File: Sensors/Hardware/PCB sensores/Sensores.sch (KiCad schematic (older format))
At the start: 49 parts, among them J1 Conn_01x02_Female, J2 Conn_01x03, J3 Conn_02x04_Top_Bottom, J4 Conn_01x02_Female, Q1 2N3904, U1 LM324, U2 LM324, U3 ADP1101, U4 MPX10DP, U5 LM358

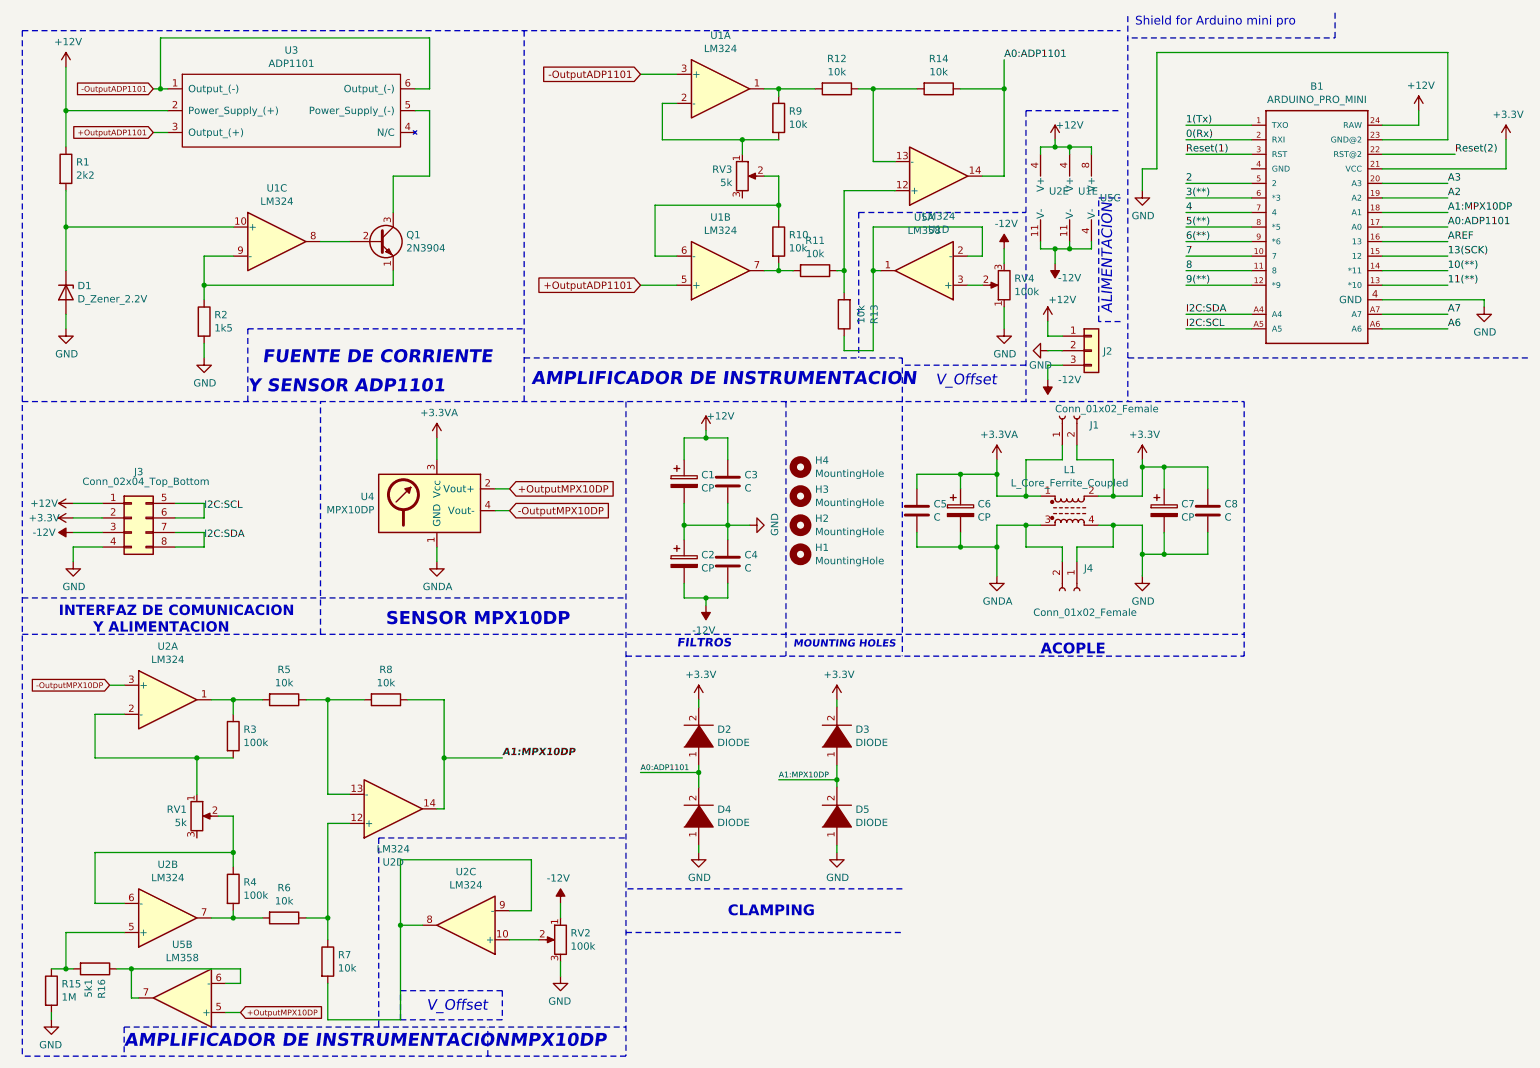
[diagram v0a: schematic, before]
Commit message: Wrapping everything up. Sensors now work fine. Preliminary PID tunning.
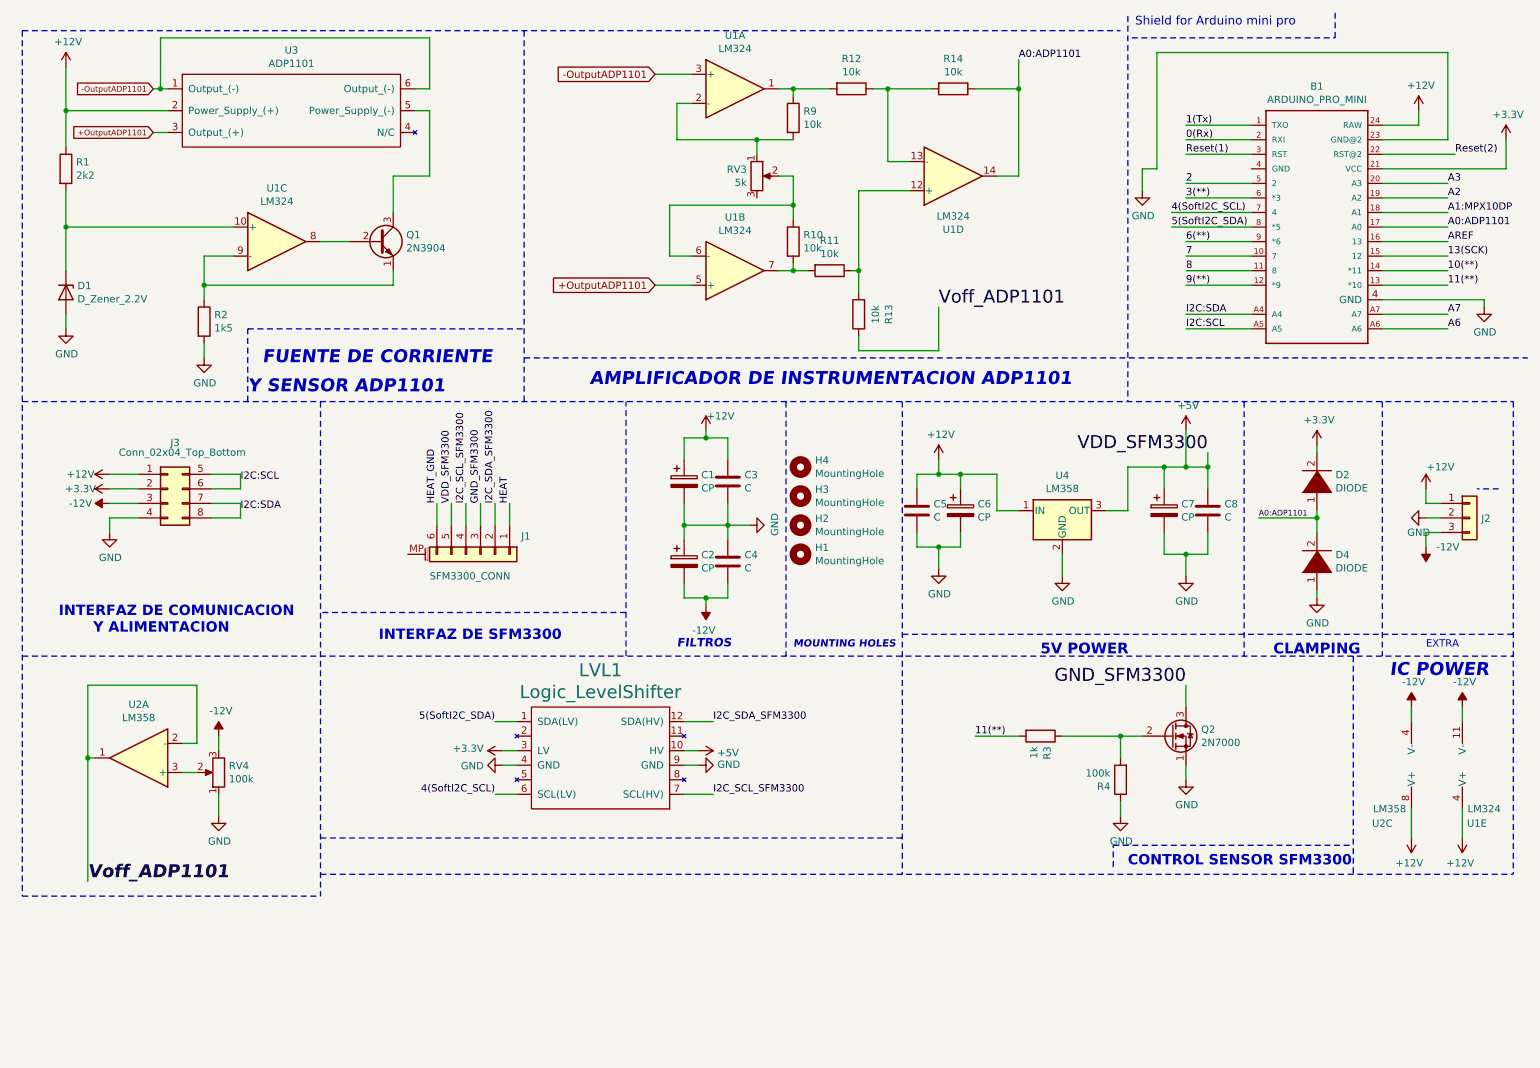
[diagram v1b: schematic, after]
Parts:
- removed D3, D5: DIODE, Diode_THT:D_A-405_P10.16mm_Horizontal, symbol pspice:DIODE
- removed J1, J4: Conn_01x02_Female, Connector_PinHeader_2.54mm:PinHeader_1x02_P2.54mm_Vertical, symbol Connector:Conn_01x02_Female
- removed L1: L_Core_Ferrite_Coupled, I_Common_M:L_CommonMode_Wuerth_WE-CMB-M, symbol Device:L_Core_Ferrite_Coupled
- removed R15: 1M, Resistor_THT:R_Axial_DIN0207_L6.3mm_D2.5mm_P10.16mm_Horizontal, symbol Device:R
- removed R16: 5k1, Resistor_THT:R_Axial_DIN0207_L6.3mm_D2.5mm_P10.16mm_Horizontal, symbol Device:R
- removed R5, R6, R7, R8: 10k, Resistor_THT:R_Axial_DIN0207_L6.3mm_D2.5mm_P10.16mm_Horizontal, symbol Device:R
- removed RV1: 5k, 3296W-1-254LF:TRIM_3296W-1-254LF, symbol Device:R_POT
- removed RV2: 100k, 3296W-1-254LF:TRIM_3296W-1-254LF, symbol Device:R_POT
- removed U2: LM324, Package_DIP:DIP-14_W7.62mm, symbol Amplifier_Operational:LM324
- removed U4: MPX10DP, MPX10DP:SIP1067W46P254L2946H2934Q4P, symbol MPX10DP:MPX10DP
- removed unit 2 of U5
- removed unit 3 of U5
- added J1: SFM3300_CONN, SFM3300:PinHeader_1x07_P2.54mm_Vertical, symbol Connector_Generic_MountingPin:Conn_01x06_MountingPin
- added LVL1: Logic_LevelShifter, Level_Shifter:Logic_LevelShifter, symbol Logic_LevelTranslator:Logic_LevelShifter
- added Q2: 2N7000, Package_TO_SOT_THT:TO-92_Inline, symbol Transistor_FET:2N7000
- added unit 3 of U2
- added U4: LM358, Package_TO_SOT_THT:TO-220-3_Vertical, symbol Regulator_Linear:L7805
- R3: value 100k -> 1k
- renumbered U5 to U2
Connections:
- net +3.3VA is gone; now on net +12V: C5.1, C6.1
- net GNDA is gone; now on net GND: C5.2, C6.2
- net +12V: now also U2.8 (V+), U4.1 (IN)
- net +3V3: now also LVL1.3 (LV); no longer C7.1, C8.1
- net -12V: now also U2.4 (V-)
- net 11(**): now also R3.2
- net GND: now also R4.1, LVL1.4 (GND), LVL1.9 (GND), Q2.1 (S), U4.2 (GND)
- net at R3.1: now also R4.2, Q2.2 (G)
- net Voff_ADP1101: now reaches R13.1, U2.1, U2.2 (-)
- net 4 renamed 4(SoftI2C_SCL)
- net 4(SoftI2C_SCL): now also LVL1.6 (SCL(LV))
- net 5(**) renamed 5(SoftI2C_SDA)
- net 5(SoftI2C_SDA): now also LVL1.1 (SDA(LV))
- new net +5V: C7.1, C8.1, J1.5 (Pin_5), LVL1.10 (HV), U4.3 (OUT)
- new net GND_SFM3300: J1.3 (Pin_3), Q2.3 (D)
- new net HEAT: J1.1 (Pin_1)
- new net HEAT_GND: J1.6 (Pin_6)
- new net I2C_SCL_SFM3300: J1.4 (Pin_4), LVL1.7 (SCL(HV))
- new net I2C_SDA_SFM3300: J1.2 (Pin_2), LVL1.12 (SDA(HV))
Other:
- note added: "5V POWER\n"
- note added: "AMPLIFICADOR DE INSTRUMENTACION ADP1101\n"
- note added: "CONTROL SENSOR SFM3300"
- note added: "EXTRA"
- note added: "IC POWER\n"
- note added: "INTERFAZ DE SFM3300\n"
- note removed: "ACOPLE\n"
- note removed: "ALIMENTACION"
- note removed: "AMPLIFICADOR DE INSTRUMENTACION"
- note removed: "MPX10DP"
- note removed: "SENSOR MPX10DP"
- note removed: "V_Offset"
- moved on the sheet: D2, D4, J2, J3, R10, R11, R12, R13, R14, R9, RV3, RV4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
